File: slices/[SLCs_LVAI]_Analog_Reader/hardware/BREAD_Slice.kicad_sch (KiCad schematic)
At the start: 85 parts

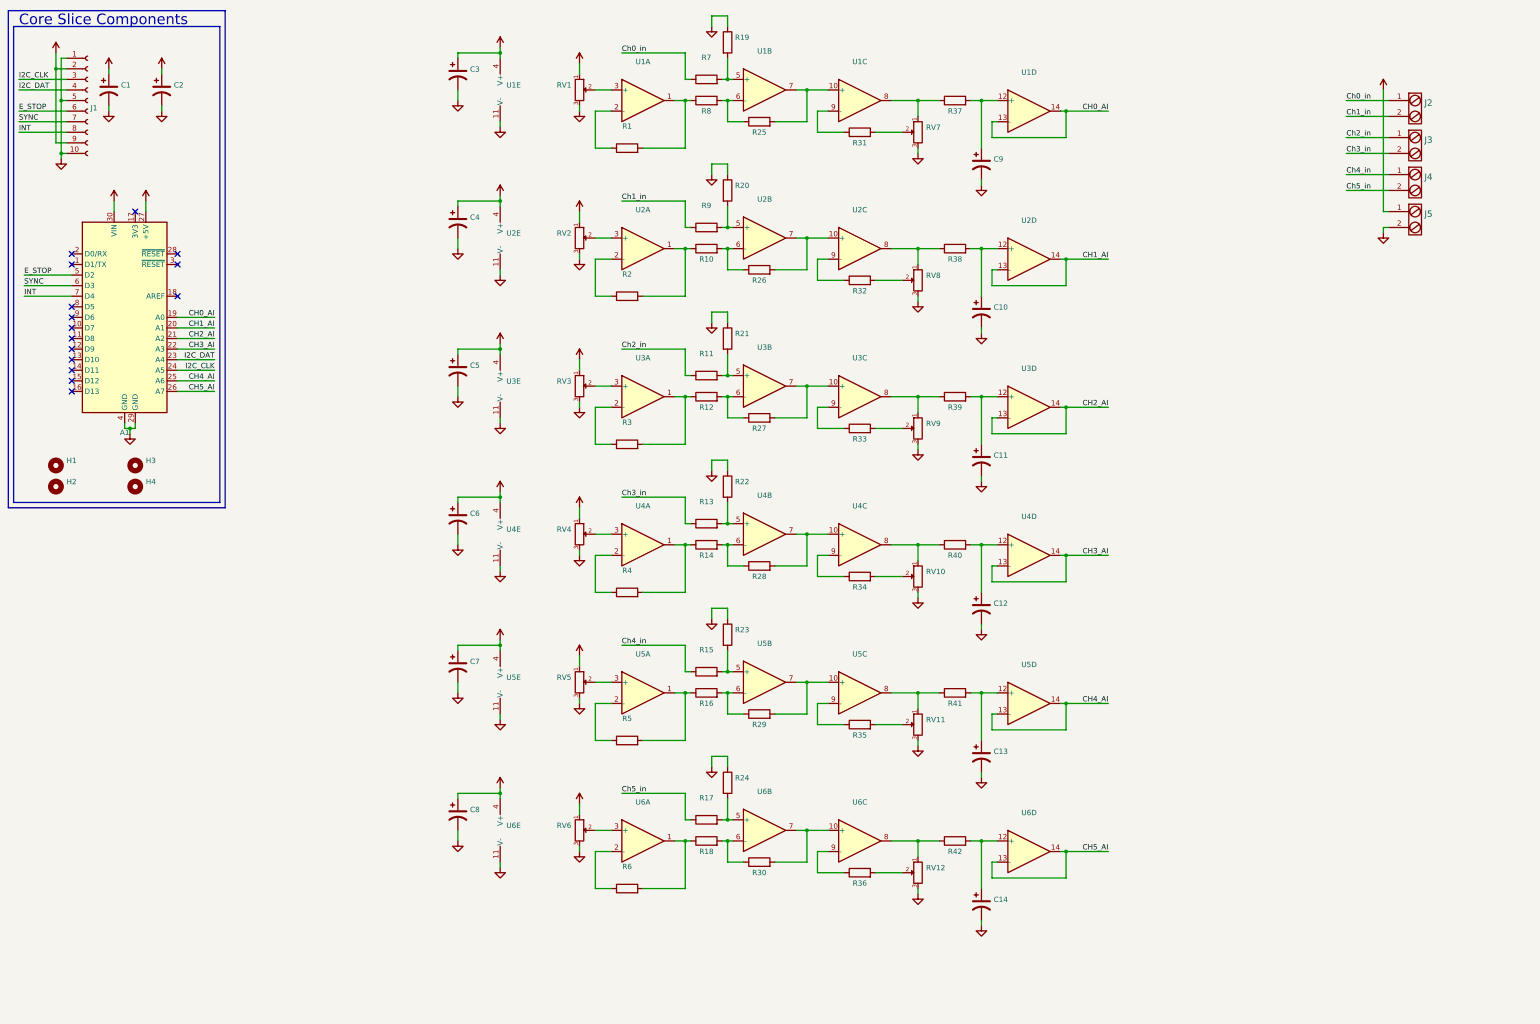
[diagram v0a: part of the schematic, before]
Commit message: restructuring for rpi boards
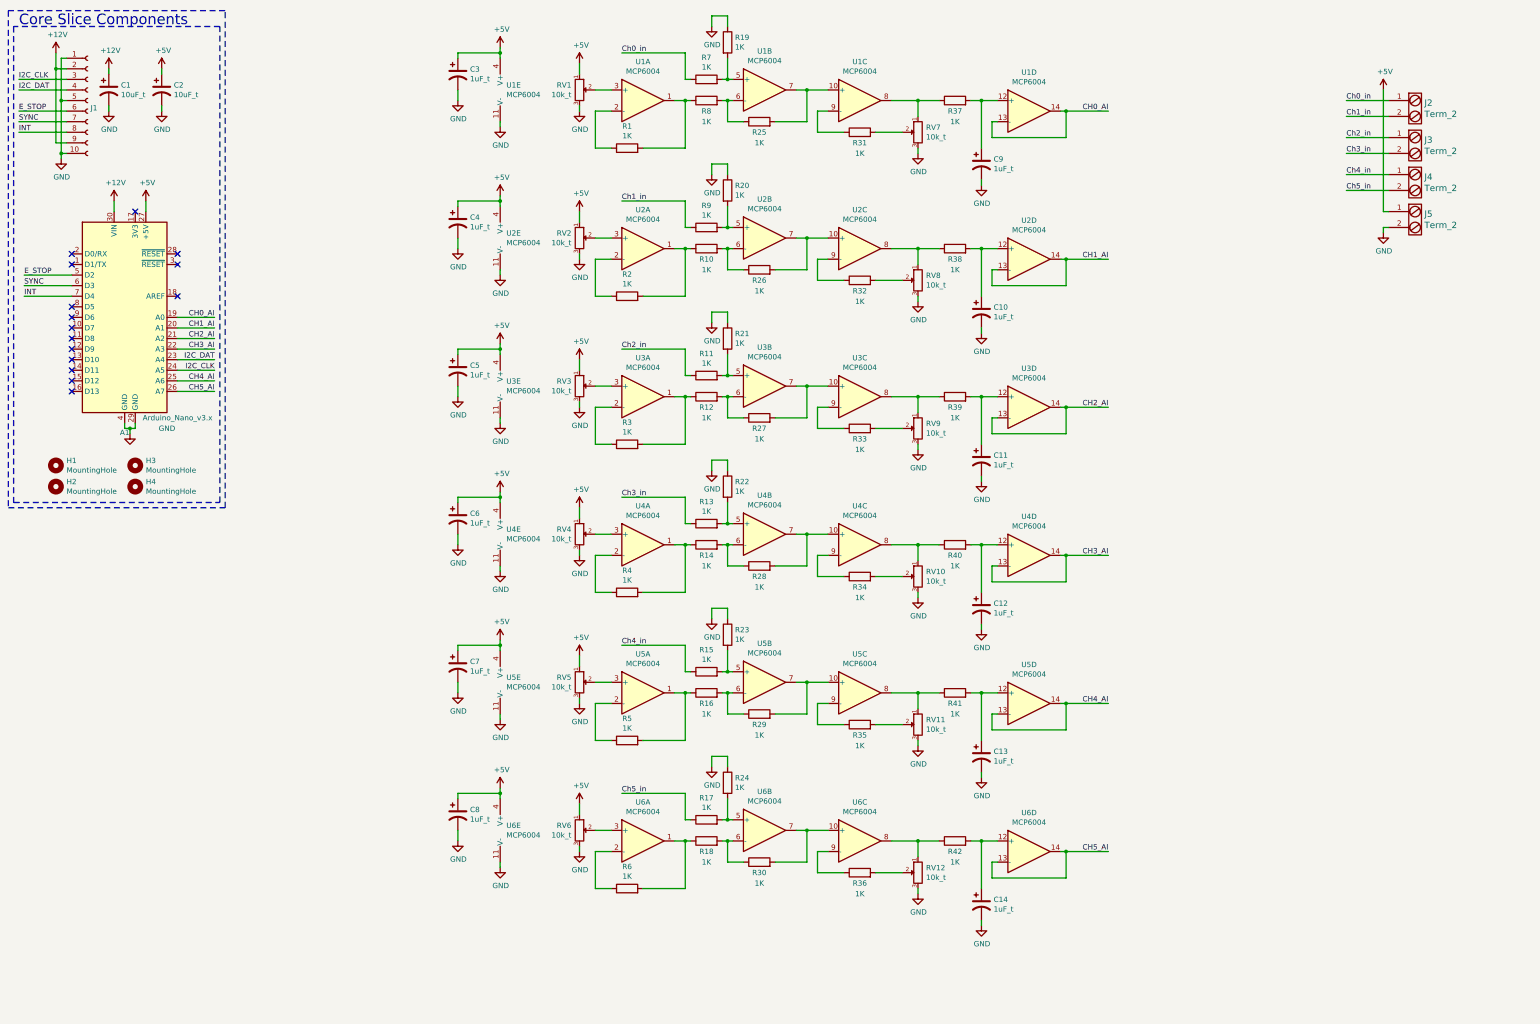
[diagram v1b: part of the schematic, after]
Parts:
- A1: value (none) -> Arduino_Nano_v3.x; footprint (none) -> Module:Arduino_Nano
- C1, C2: value (none) -> 10uF_t; footprint (none) -> OCI_UPL_FOOTPRINTS:C_2312
- C10, C11, C12, C13, C14, C3, C4, C5, C6, C7, C8, C9: value (none) -> 1uF_t; footprint (none) -> OCI_UPL_FOOTPRINTS:C_1206_HandSoldering
- H1, H2, H3, H4: value (none) -> MountingHole; footprint (none) -> MountingHole:MountingHole_3.2mm_M3_DIN965_Pad
- J1: value (none) -> Conn_01x10_Female; footprint (none) -> Connector_PinSocket_2.54mm:PinSocket_1x10_P2.54mm_Horizontal
- J2, J3, J4, J5: value (none) -> Term_2; footprint (none) -> OCI_UPL_FOOTPRINTS:TerminalBlock_Pheonix_MKDS1.5-2pol
- Logo1: value (none) -> Logo_Open_Hardware_Small; footprint (none) -> Symbol:OSHW-Symbol_6.7x6mm_SilkScreen
- R1, R10, R11, R12, R13, R14, R15, R16, R17, R18, R19, R2, R20, R21, R22, R23, R24, R25, R26, R27, R28, R29, R3, R30, R31, R32, R33, R34, R35, R36, R37, R38, R39, R4, R40, R41, R42, R5, R6, R7, R8, R9: value (none) -> 1K; footprint (none) -> OCI_UPL_FOOTPRINTS:R_1206_HandSoldering
- RV1, RV10, RV11, RV12, RV2, RV3, RV4, RV5, RV6, RV7, RV8, RV9: value (none) -> 10k_t; footprint (none) -> OCI_UPL_FOOTPRINTS:Potentiometer_Bourns_3296W_3-8Zoll_Inline_ScrewUp
- U1, U2, U3, U4, U5, U6: value (none) -> MCP6004; footprint (none) -> Package_DIP:DIP-14_W7.62mm_Socket_LongPads
